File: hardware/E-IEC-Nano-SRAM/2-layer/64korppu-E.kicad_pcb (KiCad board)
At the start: 2 copper layers, 100 x 80 mm, 41 parts, among them J1 DIN-6_IEC, J2 Floppy_34pin, J3 DC_Jack, U1 Arduino_Nano, U2 23LC256, U3 74HC595

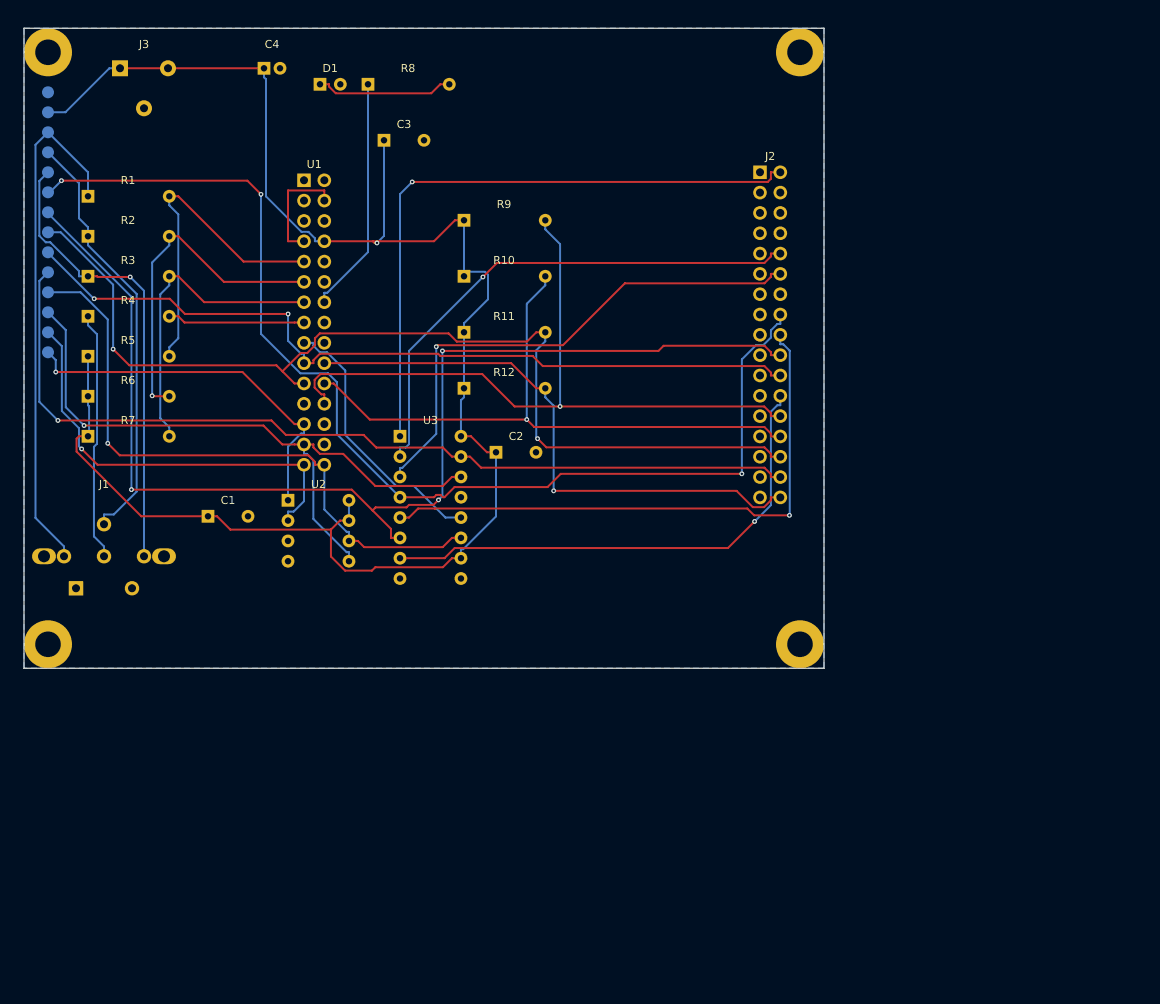
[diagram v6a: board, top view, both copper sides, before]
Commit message: Shrink 2-layer PCB from 100x80mm to 90x70mm
- Improve layout algorithm for small boards:
  resistor stacking near DIN-6, cap collision avoidance,
  adaptive test point spacing
- Board area reduced 21% (8000mm² → 6300mm²)
- DRC clean: 0 critical, 0 warnings, 0 unconnected

Co-Authored-By: Claude Opus 4.6 <noreply@anthropic.com>
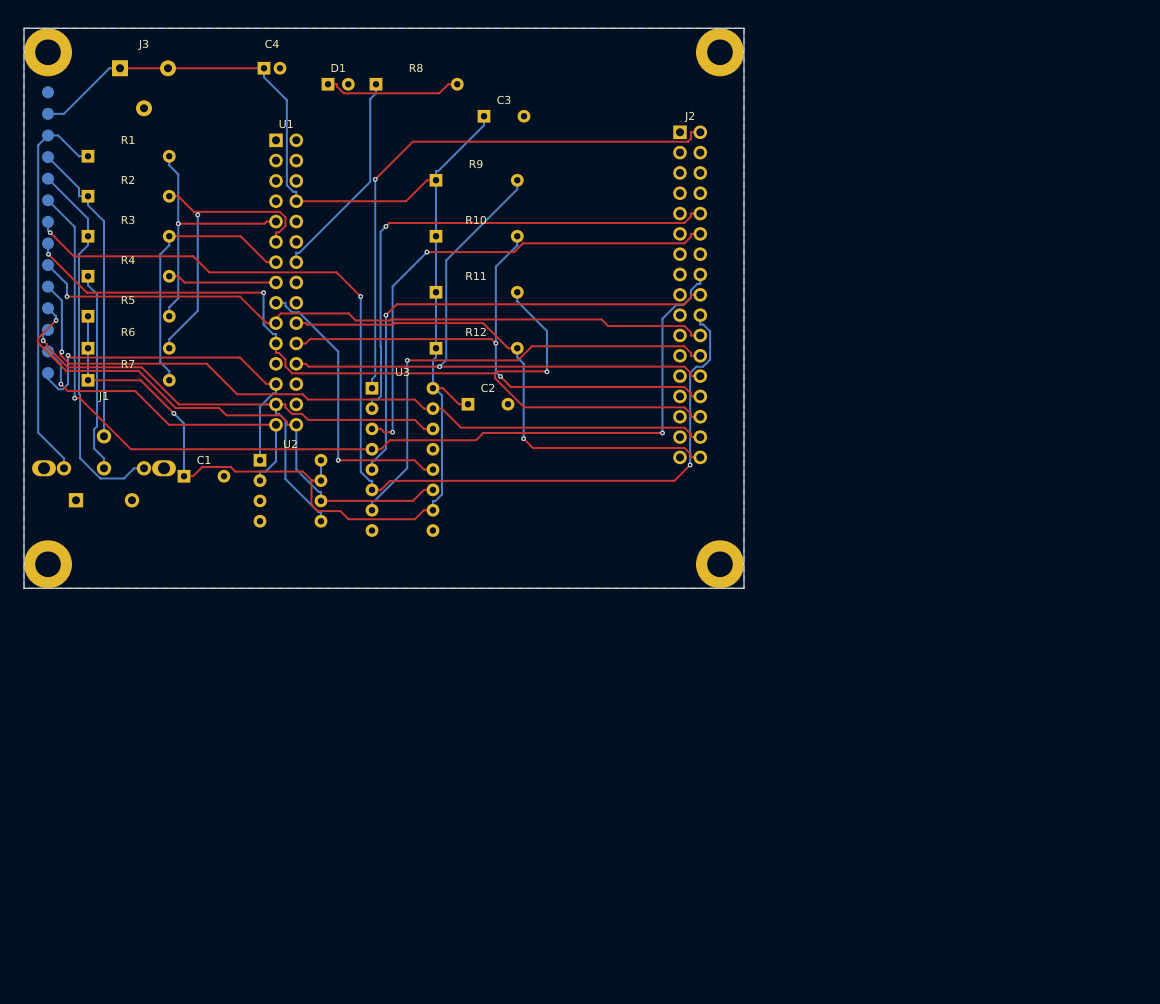
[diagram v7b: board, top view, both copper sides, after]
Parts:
- moved H4 14.1 mm to (187.0, 167.0)
- moved C3 12.9 mm to (157.5, 111.0)
- moved J2 11.2 mm to (182.0, 113.0)
- moved J1 11.0 mm to (110.0, 155.0)
- moved H2 10.0 mm to (187.0, 103.0)
- moved H3 10.0 mm to (103.0, 167.0)
- moved R7 7.00 mm to (108.0, 144.0)
- moved C2 6.95 mm to (155.5, 147.0)
- moved U3 6.95 mm to (143.5, 145.0)
- moved R10 6.10 mm to (151.5, 126.0)
- moved R11 6.10 mm to (151.5, 133.0)
- moved R12 6.10 mm to (151.5, 140.0)
- moved R9 6.10 mm to (151.5, 119.0)
- moved U1 6.10 mm to (131.5, 114.0)
- moved U2 6.10 mm to (129.5, 154.0)
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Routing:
- net +5V: track 215.1 -> 195.1 mm
- net FLOPPY_SIDE1: track 113.4 -> 93.8 mm
- net FLOPPY_MOTOR: track 141.9 -> 125.6 mm, vias 3 -> 2
- net FLOPPY_STEP: track 146.5 -> 130.5 mm
- net IEC_ATN: track 65.2 -> 49.5 mm
- net IEC_CLK: track 53.5 -> 38.5 mm
- net GND: track 14.2 -> 0.00 mm
- net FLOPPY_WDATA: track 102.0 -> 88.0 mm, vias 2 -> 1
- net FLOPPY_DIR: track 72.8 -> 60.7 mm
- net FLOPPY_RDATA: track 126.1 -> 114.2 mm, vias 2 -> 3
- net SPI_MOSI: track 84.3 -> 72.6 mm
- net SPI_MISO: track 53.2 -> 42.0 mm
- net IEC_DATA: track 57.9 -> 47.1 mm, vias 1 -> 0
- net SPI_SCK: track 78.5 -> 67.9 mm
- net FLOPPY_TRK00: track 88.7 -> 78.7 mm
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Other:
- board size 100 x 80 mm -> 90 x 70 mm
